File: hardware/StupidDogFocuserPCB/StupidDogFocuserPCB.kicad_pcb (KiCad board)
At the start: 2 copper layers, 68.6 x 53.3 mm, 18 parts, among them M1 Stepper_Motor_bipolar, SW1 Rotary_Encoder_Switch, U1 DHT11, U2 SN74HC14N

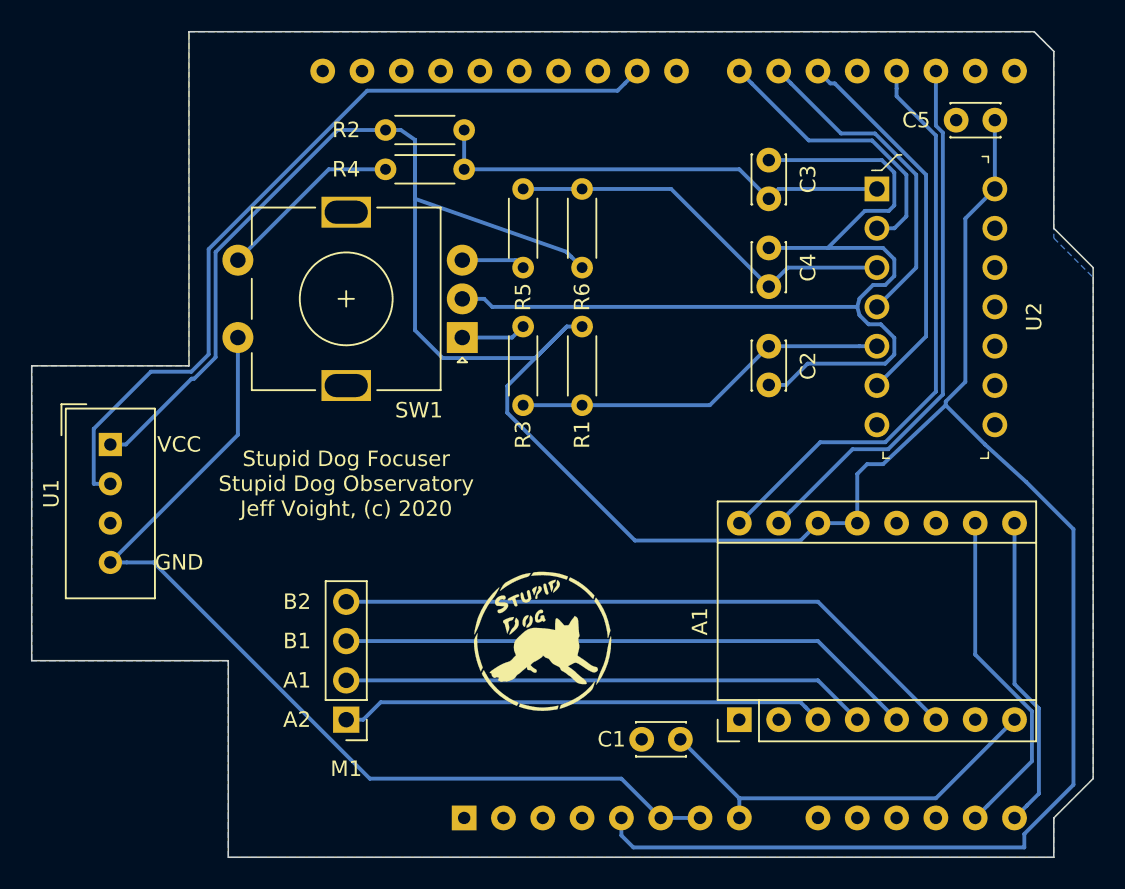
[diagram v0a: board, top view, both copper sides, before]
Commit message: Remapped kicad pins. Still need to map firmware.
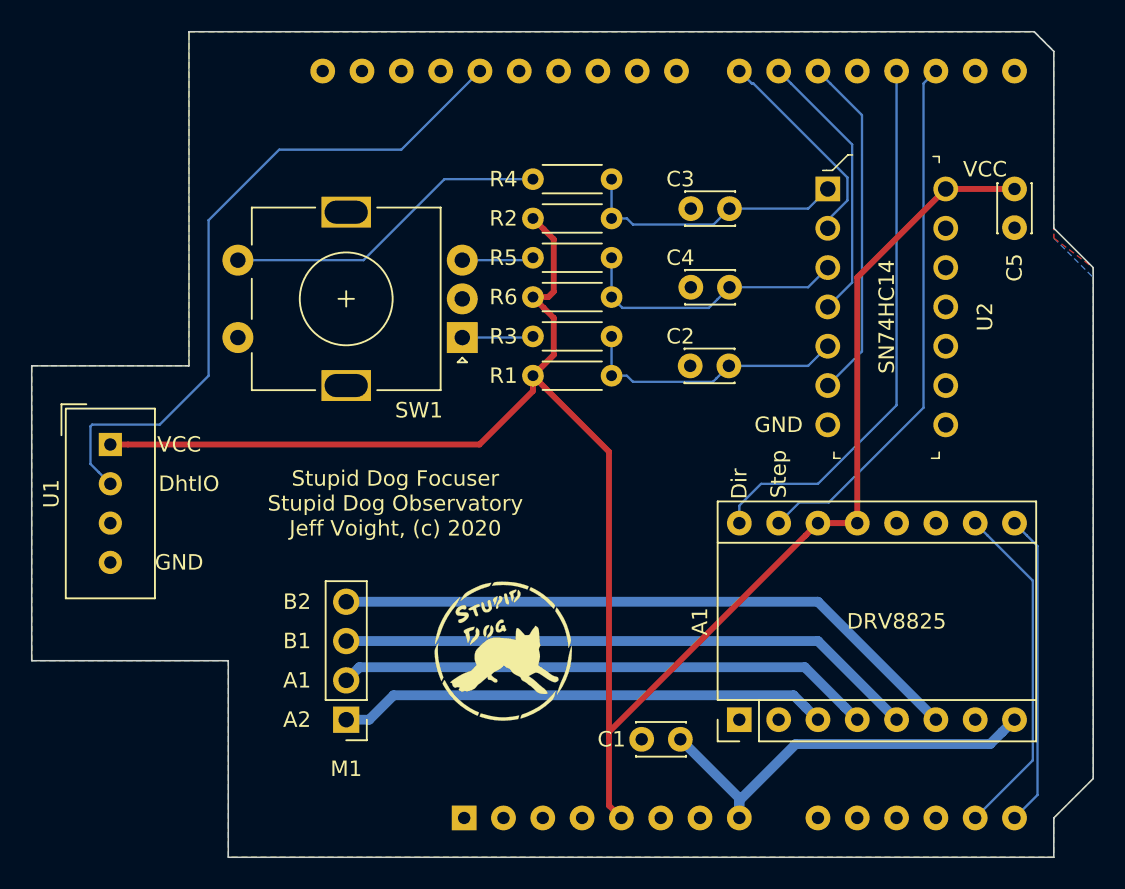
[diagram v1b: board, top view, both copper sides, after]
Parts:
- R1, R2, R3, R4, R5, R6: value R -> 1k
- moved R2 11.1 mm to (127.6, 69.2)
- moved R4 9.55 mm to (132.7, 66.7)
- moved R3 7.24 mm to (132.7, 76.8), turned to 180 degrees
- moved R6 7.24 mm to (132.7, 74.3), turned to 180 degrees
- moved C4 5.64 mm to (137.8, 73.7), turned to 0 degrees
- moved C5 4.62 mm to (158.8, 67.3), turned to 270 degrees
- moved R1 4.49 mm to (127.6, 79.4), turned to 0 degrees
- moved U2 3.18 mm to (146.7, 67.3)
- moved C2 2.88 mm to (140.3, 78.7), turned to 180 degrees
- moved G*** 2.62 mm to (125.7, 97.2)
- moved C3 2.62 mm to (140.3, 68.6), turned to 180 degrees
- moved R5 0.90 mm to (127.6, 71.8), turned to 0 degrees
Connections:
- A2 pad 24: DHT -> (no net)
- A2 pad 28: (no net) -> DHT
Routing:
- net GND: track 130.9 -> 0.00 mm
- net VCC: track 197.5 -> 124.0 mm
- net SW: track 30.3 -> 17.6 mm
- net Net-(R4-Pad2): track 12.0 -> 21.2 mm
- net DHT: track 53.3 -> 44.8 mm
- net ENC_B: track 26.0 -> 17.9 mm
- net ENC_A: track 24.4 -> 17.6 mm
- net SW_A: track 18.5 -> 13.6 mm
- net ENCB_A: track 21.3 -> 17.9 mm
- net Dir: track 38.0 -> 35.6 mm
- net ENCA_A: track 24.7 -> 22.4 mm
- net VDD: track 26.5 -> 27.7 mm
- net A1: track 34.1 -> 34.8 mm
- net Step: track 35.1 -> 34.5 mm
- net Net-(R5-Pad1): track 4.13 -> 4.63 mm
- added copper zone on F.Cu, net GND
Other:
- net class 12V added: clearance 0.4572, trace_width 0.635, via_dia 0.762, via_drill 0.3302
- net class 5V added: clearance 0.3048, trace_width 0.381, via_dia 0.6858, via_drill 0.3302
- net class Default: clearance 0.2 -> 0.1524; trace_width 0.25 -> 0.1524; via_dia 0.8 -> 0.6858; via_drill 0.4 -> 0.3302
- rule pad_to_mask_clearance: 0.051 -> 0.0508
- rule solder_mask_min_width: 0.25 -> 0.1016
- rule trace_clearance: 0.2 -> 0.1524
- rule trace_min: 0.2 -> 0.1524
- rule via_min_drill: 0.3 -> 0.254
- rule via_min_size: 0.4 -> 0.508
- board text added: "DRV8825"
- board text added: "DhtIO"
- board text added: "Dir"
- board text added: "SN74HC14"
- board text added: "Step"
